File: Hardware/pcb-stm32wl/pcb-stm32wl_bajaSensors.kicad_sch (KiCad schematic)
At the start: 0 parts

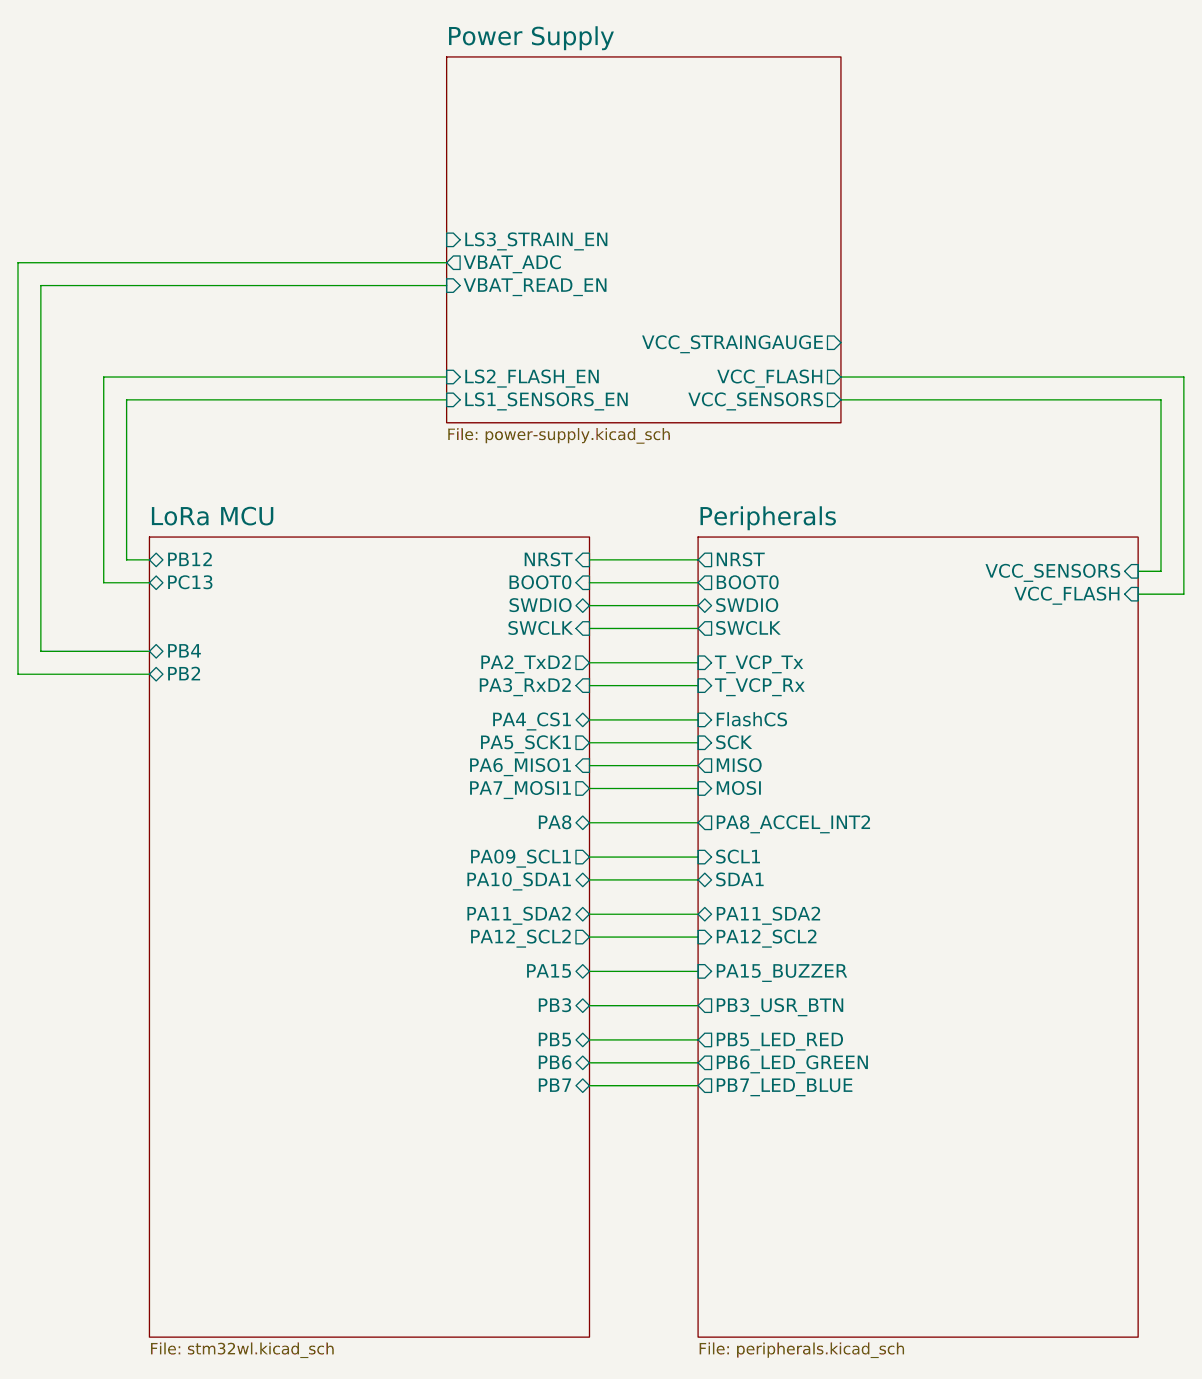
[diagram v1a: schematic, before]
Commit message: completed first attempt at wiring this horrendous adc
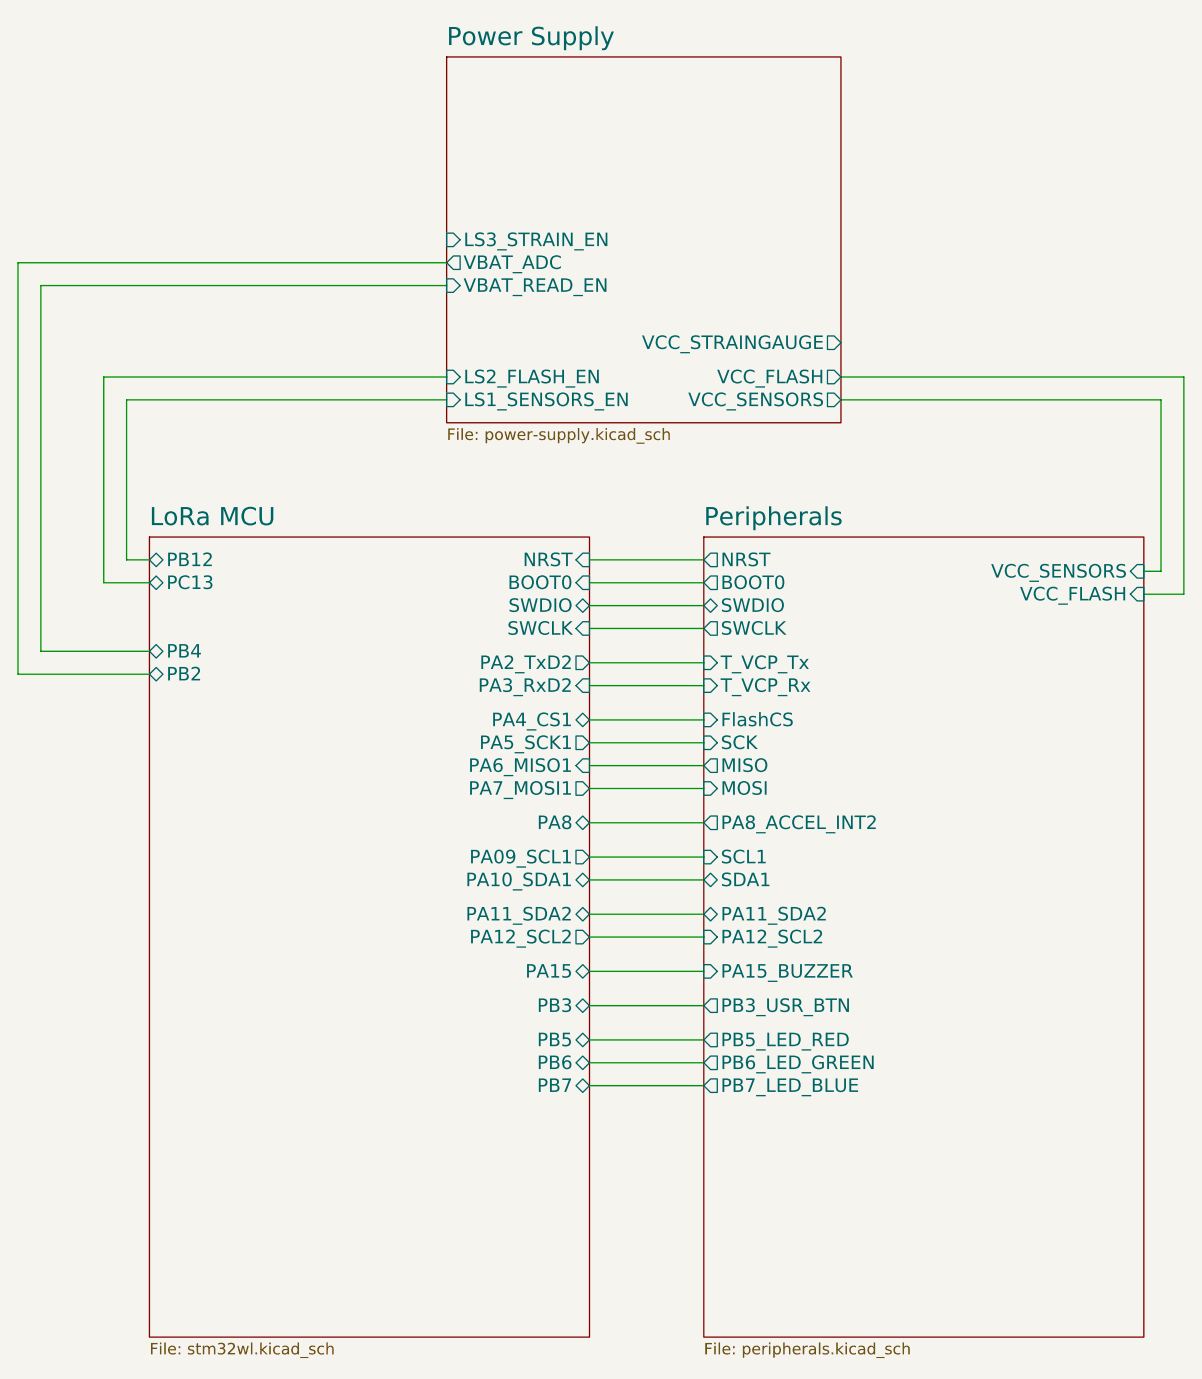
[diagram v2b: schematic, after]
